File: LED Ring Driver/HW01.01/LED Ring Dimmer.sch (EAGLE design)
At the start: 71 parts, among them IC1 TPS54202DDCR, IC2 LD1117S33TR, M1 M_HOLE_3M, M2 M_HOLE_3M, M3 M_HOLE_3M, M4 M_HOLE_3M, Q1 2N7002, U1 TPS92515QDGQTQ1DGQ0010A_M, X1 WF2549-2WS05S0B01, X2 X01_PAD-2MM, X3 X01_PAD-2MM, X4 X01_PAD-2MM, X5 X01_PAD-2MM, X6 X01_PAD-2MM, X7 PJ-057BH

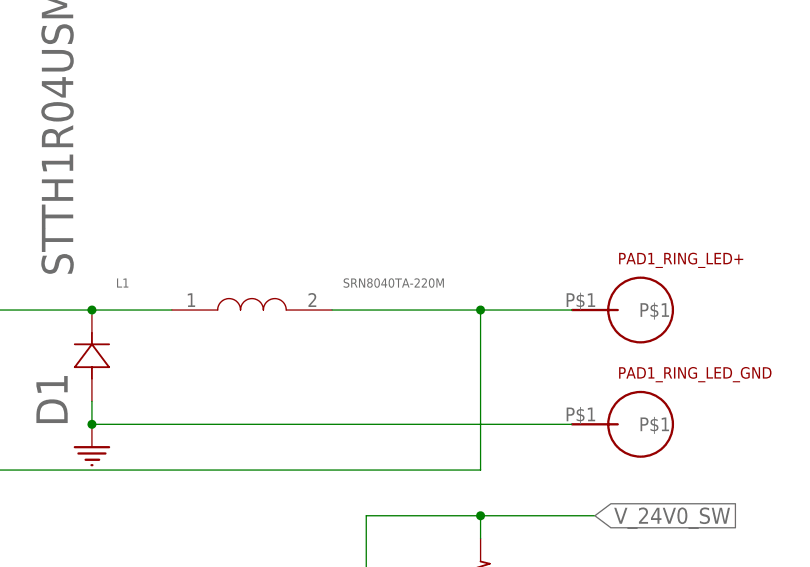
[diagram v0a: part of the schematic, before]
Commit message: HW01.01
Fixed issue of not connected 24V0 Net, and added a DC Jack Connector , On Status LED, and Switch
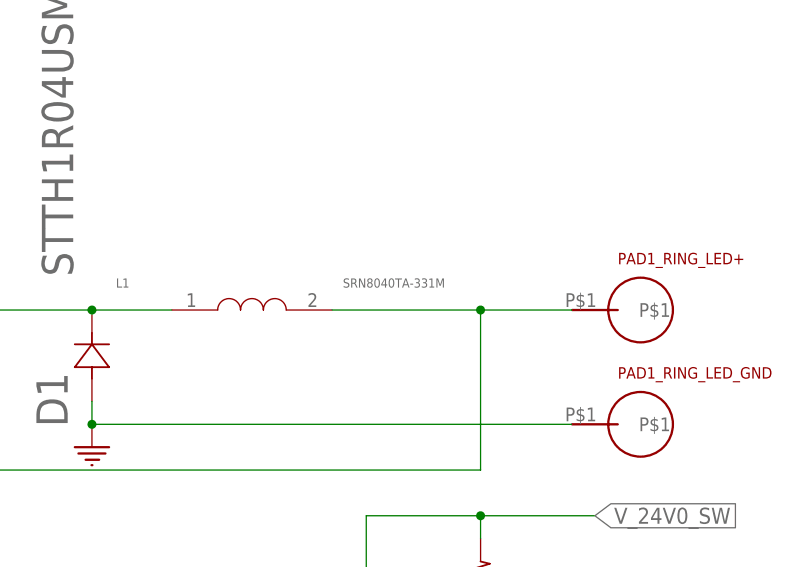
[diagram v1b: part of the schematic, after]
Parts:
- L1: value SRN8040TA-220M -> SRN8040TA-331M; device Labops_Lib_AH:SRN8040TA-220M -> Labops_Lib_AH:SRN8040TA-331M
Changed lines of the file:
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@@
 <part name="C5" library="Labops_Lib_AH" deviceset="C_0603" device="EIA0603" value="100nF/50V"/>
 <part name="D1" library="Labops_Lib_AH" deviceset="STTH1R04U" device="SMB"/>
-<part name="L1" library="Labops_Lib_AH" deviceset="SRN8040TA-220M" device=""/>
+<part name="L1" library="Labops_Lib_AH" deviceset="SRN8040TA-331M" device=""/>
 <part name="PAD1_RING_LED+" library="Labops_Lib_AH" deviceset="THT_PAD_5MM" device=""/>
 <part name="GND5" library="Labops_Lib_AH" deviceset="GND" device=""/>

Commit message: LED Ring Driver HW01.01
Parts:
- R10: value 22K 1 -> 22K 1%
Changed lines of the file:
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@@
 <setting verticaltext="up"/>
 </settings>
-<grid distance="0.1" unitdist="inch" unit="inch" style="lines" multiple="1" display="yes" altdistance="0.01" altunitdist="inch" altunit="inch"/>
+<grid distance="0.1" unitdist="inch" unit="inch" style="lines" multiple="1" display="no" altdistance="0.01" altunitdist="inch" altunit="inch"/>
 <layers>
 <layer number="1" name="Top" color="4" fill="1" visible="no" active="no"/>
@@
 <part name="C6" library="Labops_Lib_AH" deviceset="C_0603" device="EIA0603" value="100nF/50V"/>
 <part name="IC1" library="Labops_Lib_AH" deviceset="TPS54202DDCR" device=""/>
-<part name="R10" library="Labops_Lib_AH" deviceset="R_0603" device="" value="22K 1"/>
+<part name="R10" library="Labops_Lib_AH" deviceset="R_0603" device="" value="22K 1%"/>
 <part name="R11" library="Labops_Lib_AH" deviceset="R_0603" device="" value="3K01 1%"/>
 <part name="L2" library="Labops_Lib_AH" deviceset="SRN8040TA-220M" device=""/>
